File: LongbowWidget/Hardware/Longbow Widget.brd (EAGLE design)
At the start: 30.2 x 18 mm, 29 parts, among them J0 CONN_6SCREW_2.54, J1 CONN_6SCREW_2.54, Q2 DMG3404, U1 TPS7A0533DBV, U2 SN65HVD33RHL

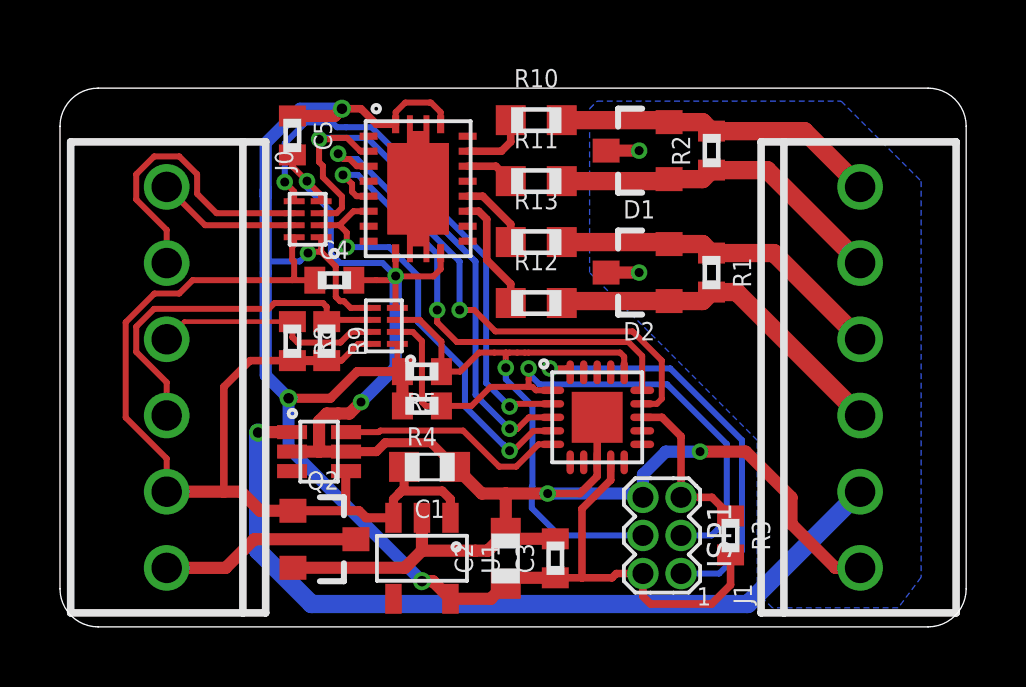
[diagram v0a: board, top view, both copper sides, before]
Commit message: Updated to v0.3
Minor update, added jumpers to allow for conversion to 2 wire RS485 without external jumping/connection. Made edits in Eagle, generated new gerber files and updated BoM to reflect "jumper" parts
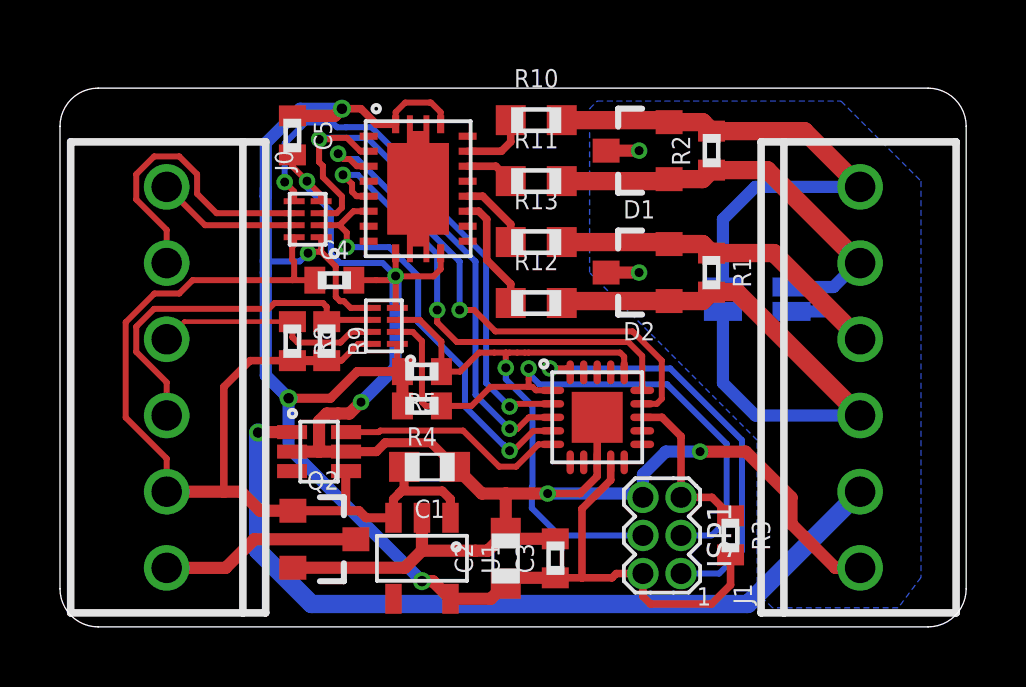
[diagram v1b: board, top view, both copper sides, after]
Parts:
- added JP1, JP2: JUMPER-SMT_2_NO_SILK, SparkFun-Jumpers:SMT-JUMPER_2_NO_SILK
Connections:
- net RX+: now also JP1.1
- net RX-: now also JP2.1
- net TX+: now also JP1.2
- net TX-: now also JP2.2
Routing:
- net TX+: track 11.8 -> 19.2 mm
- net RX+: track 10.9 -> 18.1 mm
- net TX-: track 11.3 -> 14.0 mm
- net RX-: track 11.4 -> 14.0 mm
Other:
- board text added: "J1"
- board text added: "J2"
- board text added: "Longbow Widget v0.3 -------------- Designed by Northern Widget and University of Minnesota"
- board text removed: "Longbow Widget v0.2 -------------- Designed by Northern Widget and University of Minnesota"
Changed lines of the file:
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@@
 <?xml version="1.0" encoding="utf-8"?>
 <!DOCTYPE eagle SYSTEM "eagle.dtd">
-<eagle version="9.2.1">
+<eagle version="9.5.2">
 <drawing>
 <settings>
@@
 <layer number="14" name="Route14" color="1" fill="6" visible="no" active="no"/>
 <layer number="15" name="Route15" color="4" fill="6" visible="no" active="no"/>
-<layer number="16" name="Bottom" color="1" fill="1" visible="yes" active="yes"/>
+<layer number="16" name="Bottom" color="1" fill="1" visible="no" active="yes"/>
 <layer number="17" name="Pads" color="2" fill="1" visible="yes" active="yes"/>
 <layer number="18" name="Vias" color="2" fill="1" visible="yes" active="yes"/>
@@
 <layer number="20" name="Dimension" color="24" fill="1" visible="yes" active="yes"/>
 <layer number="21" name="tPlace" color="7" fill="1" visible="yes" active="yes"/>
-<layer number="22" name="bPlace" color="7" fill="1" visible="yes" active="yes"/>
+<layer number="22" name="bPlace" color="7" fill="1" visible="no" active="yes"/>
 <layer number="23" name="tOrigins" color="15" fill="1" visible="yes" active="yes"/>
-<layer number="24" name="bOrigins" color="15" fill="1" visible="yes" active="yes"/>
-<layer number="25" name="tNames" color="7" fill="1" visible="no" active="yes"/>
+<layer number="24" name="bOrigins" color="15" fill="1" visible="no" active="yes"/>
+<layer number="25" name="tNames" color="7" fill="1" visible="yes" active="yes"/>
 <layer number="26" name="bNames" color="7" fill="1" visible="no" active="yes"/>
 <layer number="27" name="tValues" color="7" fill="1" visible="no" active="yes"/>
@@
 <layer number="38" name="bTest" color="7" fill="1" visible="no" active="yes"/>
 <layer number="39" name="tKeepout" color="4" fill="11" visible="yes" active="yes"/>
-<layer number="40" name="bKeepout" color="1" fill="11" visible="yes" active="yes"/>
+<layer number="40" name="bKeepout" color="1" fill="11" visible="no" active="yes"/>
 <layer number="41" name="tRestrict" color="4" fill="10" visible="yes" active="yes"/>
-<layer number="42" name="bRestrict" color="1" fill="10" visible="yes" active="yes"/>
+<layer number="42" name="bRestrict" color="1" fill="10" visible="no" active="yes"/>
 <layer number="43" name="vRestrict" color="2" fill="10" visible="no" active="yes"/>
 <layer number="44" name="Drills" color="7" fill="1" visible="no" active="yes"/>
-<layer number="45" name="Holes" color="7" fill="1" visible="yes" active="yes"/>
+<layer number="45" name="Holes" color="7" fill="1" visible="no" active="yes"/>
 <layer number="46" name="Milling" color="3" fill="1" visible="no" active="yes"/>
 <layer number="47" name="Measures" color="7" fill="1" visible="no" active="yes"/>
-<layer number="48" name="Document" color="7" fill="1" visible="yes" active="yes"/>
+<layer number="48" name="Document" color="7" fill="1" visible="no" active="yes"/>
 <layer number="49" name="Reference" color="7" fill="1" visible="no" active="yes"/>
 <layer number="50" name="dxf" color="7" fill="1" visible="no" active="no"/>
 <layer number="51" name="tDocu" color="7" fill="1" visible="yes" active="yes"/>
-<layer number="52" name="bDocu" color="7" fill="1" visible="yes" active="yes"/>
+<layer number="52" name="bDocu" color="7" fill="1" visible="no" active="yes"/>
 <layer number="53" name="tGND_GNDA" color="7" fill="1" visible="no" active="no"/>
 <layer number="54" name="bGND_GNDA" color="7" fill="1" visible="no" active="no"/>
@@
 <text x="8.255" y="26.4795" size="0.8128" layer="52" font="vector" ratio="15" rot="MR0" align="center">To Logger</text>
 <text x="10.287" y="20.701" size="0.8128" layer="52" font="vector" ratio="15" rot="MR270" align="center">3.3v ~ 5v</text>
-<text x="27.305" y="23.241" size="0.6096" layer="52" font="vector" ratio="15" rot="MR0" align="center-left">Longbow Widget v0.2
+<text x="27.305" y="24.765" size="0.6096" layer="52" font="vector" ratio="15" rot="MR0" align="center-left">Longbow Widget v0.3
 --------------
 Designed by
@@
 <dimension x1="25.781" y1="27.686" x2="25.908" y2="9.779" x3="40.894" y3="18.7325" textsize="1.778" layer="48" dtype="vertical"/>
 <dimension x1="34.925" y1="17.653" x2="4.699" y2="20.447" x3="19.812" y3="34.544" textsize="1.778" layer="48" dtype="horizontal"/>
+<text x="26.797" y="18.923" size="1.016" layer="52" font="vector" ratio="15" rot="MR0" align="center">J1</text>
+<text x="29.083" y="18.923" size="1.016" layer="52" font="vector" ratio="15" rot="MR0" align="center">J2</text>
 </plain>
 <attributes>
@@
 </element>
 <element name="U1" library="bschulz" package="SOT23-5" value="TPS7A0533DBV" x="16.764" y="12.065" smashed="yes" rot="R180">
-<attribute name="DIGIKEY" value="" x="16.764" y="12.065" size="1.778" layer="27" rot="R180" display="off"/>
+<attribute name="DIGIKEY" value="296-TPS7A0533PDBVRCT-ND" x="16.764" y="12.065" size="1.778" layer="27" rot="R180" display="off"/>
 <attribute name="MF" value="TI" x="16.764" y="12.065" size="1.778" layer="27" rot="R180" display="off"/>
 <attribute name="MOUSER" value="595-TPS7A0533PDBVR" x="16.764" y="12.065" size="1.778" layer="27" rot="R180" display="off"/>
@@
 </element>
 <element name="U$4" library="awickert" package="NWLOGO_MED" value="NWLOGO_MED" x="15.24" y="15.24" smashed="yes" rot="MR0"/>
+<element name="JP1" library="SparkFun-Jumpers" library_urn="urn:adsk.eagle:library:528" package="SMT-JUMPER_2_NO_SILK" package3d_urn="urn:adsk.eagle:package:39279/1" value="JUMPER-SMT_2_NO_SILK" x="26.797" y="20.701" smashed="yes" rot="MR270">
+<attribute name="NAME" x="25.654" y="20.701" size="0.6096" layer="26" font="vector" ratio="20" rot="MR270" align="bottom-center"/>
+<attribute name="VALUE" x="27.94" y="20.701" size="0.6096" layer="28" font="vector" ratio="20" rot="MR270" align="top-center"/>
+</element>
+<element name="JP2" library="SparkFun-Jumpers" library_urn="urn:adsk.eagle:library:528" package="SMT-JUMPER_2_NO_SILK" package3d_urn="urn:adsk.eagle:package:39279/1" value="JUMPER-SMT_2_NO_SILK" x="29.083" y="20.701" smashed="yes" rot="MR270">
+<attribute name="NAME" x="27.94" y="20.701" size="0.6096" layer="26" font="vector" ratio="20" rot="MR270" align="bottom-center"/>
+<attribute name="VALUE" x="30.226" y="20.701" size="0.6096" layer="28" font="vector" ratio="20" rot="MR270" align="top-center"/>
+</element>
 </elements>
 <signals>
@@
 <wire x1="26.416" y1="20.94" x2="27.254821875" y2="20.94" width="0.6096" layer="1"/>
 <wire x1="27.254821875" y1="20.94" x2="31.369" y2="16.825821875" width="0.6096" layer="1"/>
+<contactref element="JP1" pad="2"/>
+<wire x1="31.369" y1="16.825821875" x2="27.878178125" y2="16.825821875" width="0.4064" layer="16"/>
+<wire x1="26.797" y1="17.907" x2="26.797" y2="20.2946" width="0.4064" layer="16"/>
+<wire x1="27.878178125" y1="16.825821875" x2="26.797" y2="17.907" width="0.4064" layer="16"/>
 </signal>
 <signal name="TX-">
@@
 <wire x1="26.416" y1="22.24" x2="28.494821875" y2="22.24" width="0.6096" layer="1"/>
 <wire x1="28.494821875" y1="22.24" x2="31.369" y2="19.365821875" width="0.6096" layer="1"/>
+<contactref element="JP2" pad="2"/>
+<wire x1="31.369" y1="19.365821875" x2="31.369" y2="19.4056" width="0.4064" layer="16"/>
+<wire x1="31.369" y1="19.4056" x2="30.48" y2="20.2946" width="0.4064" layer="16"/>
+<wire x1="30.48" y1="20.2946" x2="29.083" y2="20.2946" width="0.4064" layer="16"/>
 </signal>
 <signal name="RX-">
@@
 <wire x1="26.416" y1="25.004" x2="28.270821875" y2="25.004" width="0.6096" layer="1"/>
 <wire x1="28.270821875" y1="25.004" x2="31.369" y2="21.905821875" width="0.6096" layer="1"/>
+<contactref element="JP2" pad="1"/>
+<wire x1="31.369" y1="21.905821875" x2="31.278421875" y2="21.905821875" width="0.4064" layer="16"/>
+<wire x1="31.278421875" y1="21.905821875" x2="30.48" y2="21.1074" width="0.4064" layer="16"/>
+<wire x1="30.48" y1="21.1074" x2="29.083" y2="21.1074" width="0.4064" layer="16"/>
 </signal>
 <signal name="RX+">
@@
 <wire x1="26.416" y1="26.304" x2="29.510821875" y2="26.304" width="0.6096" layer="1"/>
 <wire x1="29.510821875" y1="26.304" x2="31.369" y2="24.445821875" width="0.6096" layer="1"/>
+<contactref element="JP1" pad="1"/>
+<wire x1="31.369" y1="24.445821875" x2="27.874821875" y2="24.445821875" width="0.4064" layer="16"/>
+<wire x1="26.797" y1="23.368" x2="26.797" y2="21.1074" width="0.4064" layer="16"/>
+<wire x1="27.874821875" y1="24.445821875" x2="26.797" y2="23.368" width="0.4064" layer="16"/>
 </signal>
 <signal name="MISO">
@@
 which will not be processed correctly with this version.
 </note>
+<note version="8.2" severity="warning">
+Since Version 8.2, EAGLE supports online libraries. The ids
+of those online libraries will not be understood (or retained)
+with this version.
+</note>
+<note version="8.3" severity="warning">
+Since Version 8.3, EAGLE supports URNs for individual library
+assets (packages, symbols, and devices). The URNs of those assets
+will not be understood (or retained) with this version.
+</note>
+<note version="8.3" severity="warning">
+Since Version 8.3, EAGLE supports the association of 3D packages
+with devices in libraries, schematics, and board files. Those 3D
+packages will not be understood (or retained) with this version.
+</note>
 </compatibility>
